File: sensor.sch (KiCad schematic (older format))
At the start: 82 parts, among them CON1 Micro USB, CON2 PROG, CON3 Jack-DC, Q1 BSS214N, Q2 BSS214N, Q3 BSS214N, Q4 BSS214N, Q5 BSS214N, Q6 BSS214N, SW1 RESET, SW2 CFG, U1 LM7805, U2 TLV1117LV33DCY, U3 ESP-12F, U4 HTU21D, U5 PMS7003

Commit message: Schematic finishing and cleanup.
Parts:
- added CON5: Conn_01x08, Connectors_Molex:Molex_PicoBlade_53048-0810_08x1.25mm_Angled, symbol Conn_01x08
- CON2: footprint Pin_Headers:Pin_Header_Angled_1x05_Pitch2.54mm -> Pin_Headers:Pin_Header_Straight_1x05_Pitch2.54mm
- CON3: footprint (none) -> Connectors:BARREL_JACK
- CON4: renamed from J?; footprint (none) -> Pin_Headers:Pin_Header_Straight_1x04_Pitch2.54mm
- SW1, SW2: footprint (none) -> Buttons_Switches_SMD:SW_SPST_EVQQ2
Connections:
- net +5V: now also CON5.1 (Pin_1)
- net GND: now also CON5.2 (Pin_2)
- net PMS_RXD: now also CON5.4 (Pin_4)
- net PMS_TXD: now also CON5.5 (Pin_5)
- net PMS_SET: now reaches R39.2, TP2.1, U5.10 (SET)
- net PMS_SET: now also CON5.3 (Pin_3)
- net PMS_RESET: now reaches R41.2, TP3.1, U5.5 (RESET)
- net PMS_RESET: now also CON5.6 (Pin_6)
- no-connect marks 9 -> 11
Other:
- note added: "Alternative connector for \nHTU21D module, can be used\nif assembling board by hand."
- note added: "Buttons"
- note added: "Connector for alternative\nPMS5003 sensor. Molex\n1.25mm PicoBlade\n530480810 or 530470810"
- note added: "HTU21D, HDC1080, Si7020 can be used.\nAccording to datasheet , central pad \nshould be left floating.\nCurrent consumption negligible."
- note added: "Humidity and temperature sensor"
- note added: "LEDs"
- note added: "Max 20mA per single LED @ minimum LED forward voltage and supply 5V+5%.\nMax. total current 200mA for one color, 600mA for all total on, but software\nlimited to 200mA max."
- note added: "Optional power supply input"
- note added: "Particulate matter sensor"
- note added: "Power supply"
- note added: "Programming connector"
- note added: "WiFi/processing module"
- note removed: "Alternative connector"
- note removed: "Humidity and temperature sensor.\nHTU21D, HDC1080, Si7020 can be used.\nAccording to datasheet , central pad \nshould be left floating.\nCurrent consumption negligible."
- note removed: "Max 20mA per single LED @ minimum LED forward voltage and supply 5V+5%.\nMax. total current 200mA for one color, 600mA for all total on."
- moved on the sheet: C1, C2, C3, C4, C5, C6, C7, C8, C9, CON1, CON2, CON3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

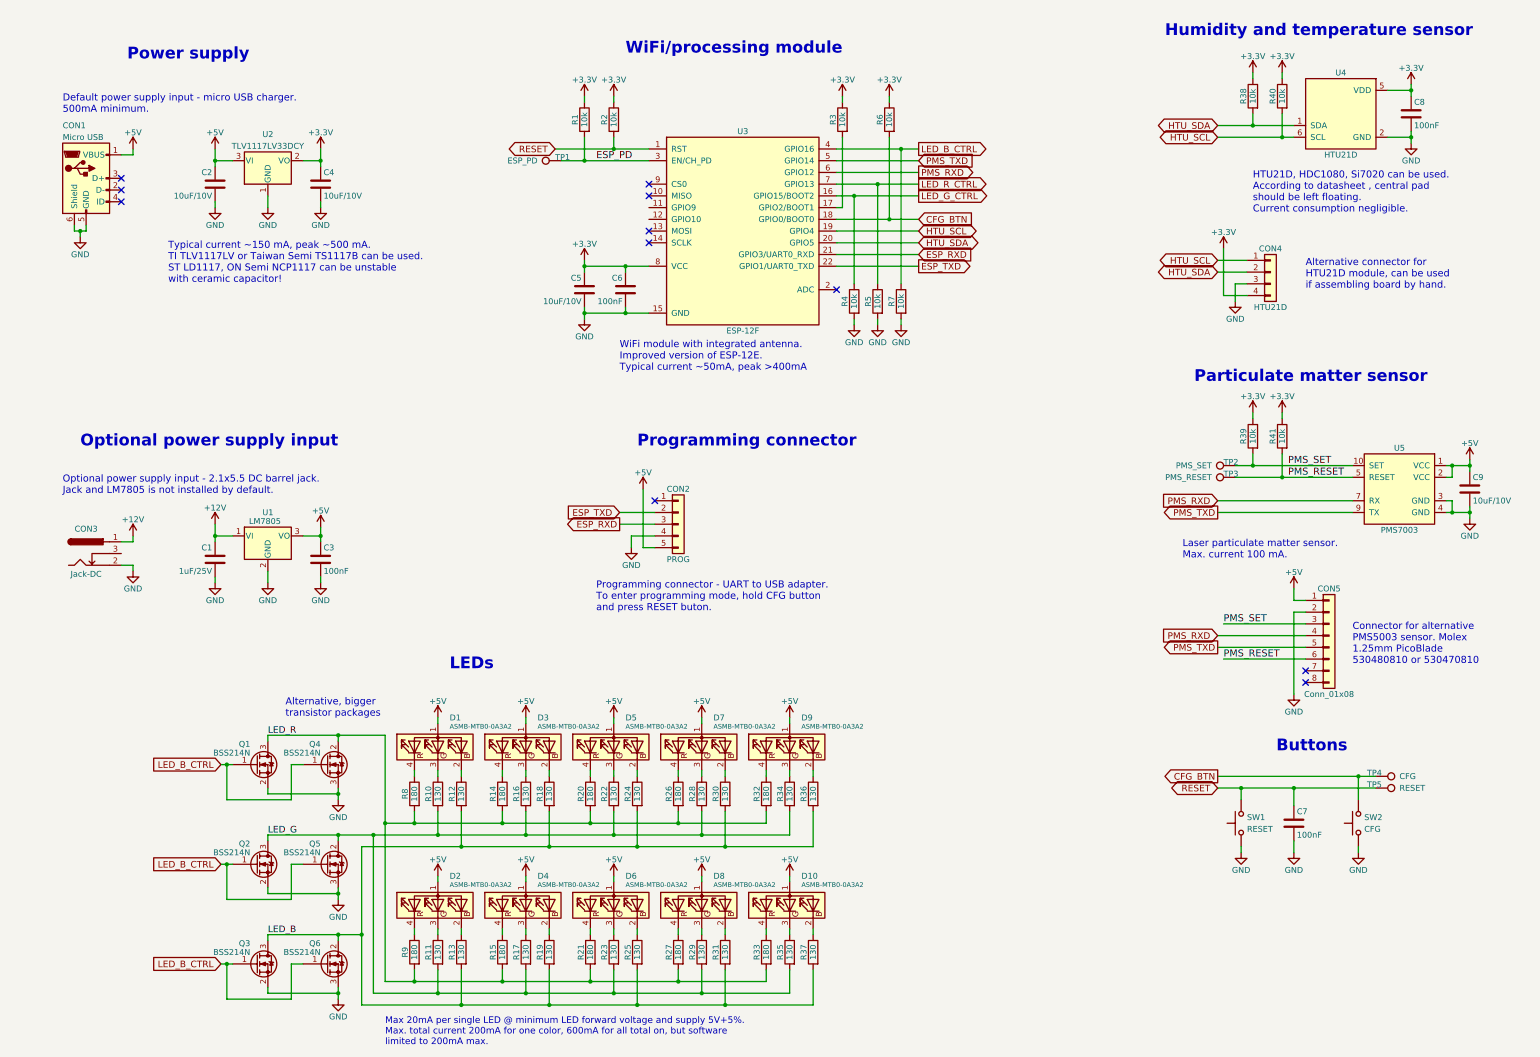
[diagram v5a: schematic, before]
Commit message: Fix ERC errors, add more testpoints.
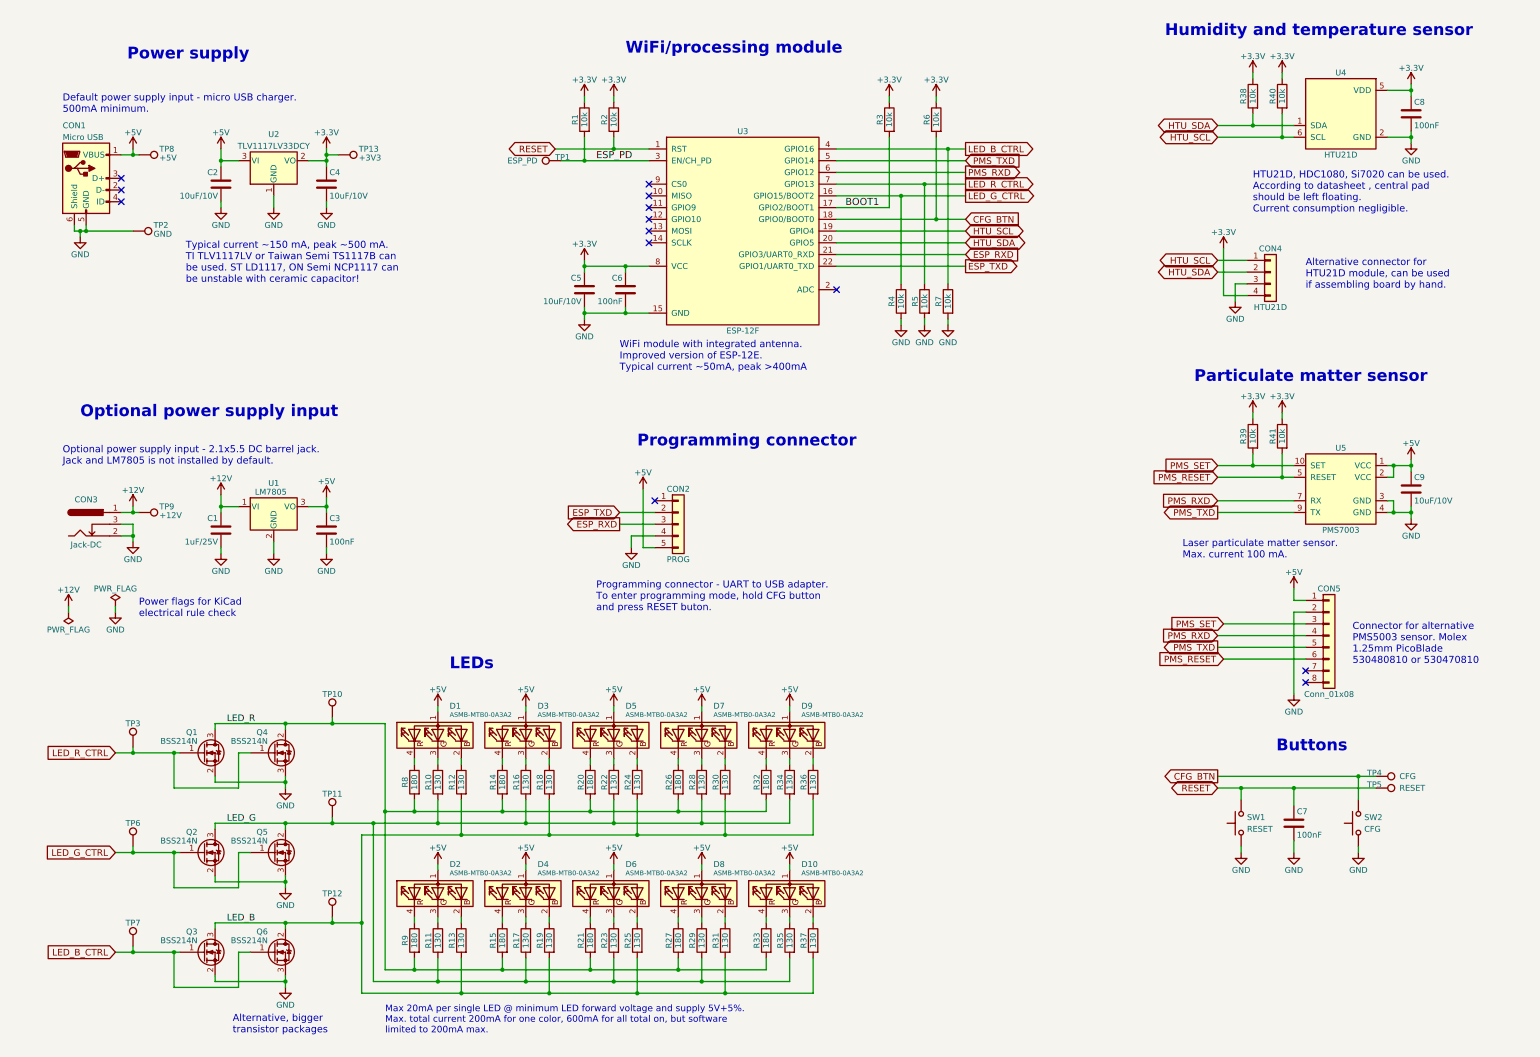
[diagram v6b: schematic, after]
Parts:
- added TP10, TP11, TP12, TP6, TP7: -, Wire_Pads:SolderWirePad_single_0-8mmDrill, symbol TEST_1P
- added TP13: +3V3, Wire_Pads:SolderWirePad_single_0-8mmDrill, symbol TEST_1P
- added TP8: +5V, Wire_Pads:SolderWirePad_single_0-8mmDrill, symbol TEST_1P
- added TP9: +12V, Wire_Pads:SolderWirePad_single_0-8mmDrill, symbol TEST_1P
- TP2: value PMS_SET -> GND
- TP3: value PMS_RESET -> -
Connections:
- net +12V: now also TP9.1
- net +3V3: now also TP13.1
- net +5V: now also TP8.1
- net GND: now also CON3.3, TP2.1
- net LED_B: now also TP12.1
- net LED_B_CTRL: now also TP7.1; no longer Q1.1 (G), Q2.1 (G), Q4.1 (G), Q5.1 (G)
- net LED_G: now also TP11.1
- net LED_G_CTRL: now also Q2.1 (G), Q5.1 (G), TP6.1
- net LED_R: now also TP10.1
- net LED_R_CTRL: now also Q1.1 (G), Q4.1 (G), TP3.1
- net PMS_RESET: no longer TP3.1
- net PMS_SET: no longer TP2.1
- net BOOT1: now reaches R3.2, U3.17 (GPIO2/BOOT1)
- no-connect marks 11 -> 13
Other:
- note added: "Power flags for KiCad\nelectrical rule check"
- note added: "Typical current ~~150 mA, peak ~~500 mA.\nTI TLV1117LV or Taiwan Semi TS1117B can \nbe used. ST LD1117, ON Semi NCP1117 can \nbe unstable with ceramic capacitor!"
- note removed: "Typical current ~~150 mA, peak ~~500 mA.\nTI TLV1117LV or Taiwan Semi TS1117B can be used.\nST LD1117, ON Semi NCP1117 can be unstable \nwith ceramic capacitor!"
- moved on the sheet: C1, C2, C3, C4, C9, CON3, D1, D10, D2, D3, D4, D5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

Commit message: Initial draft PCB placement
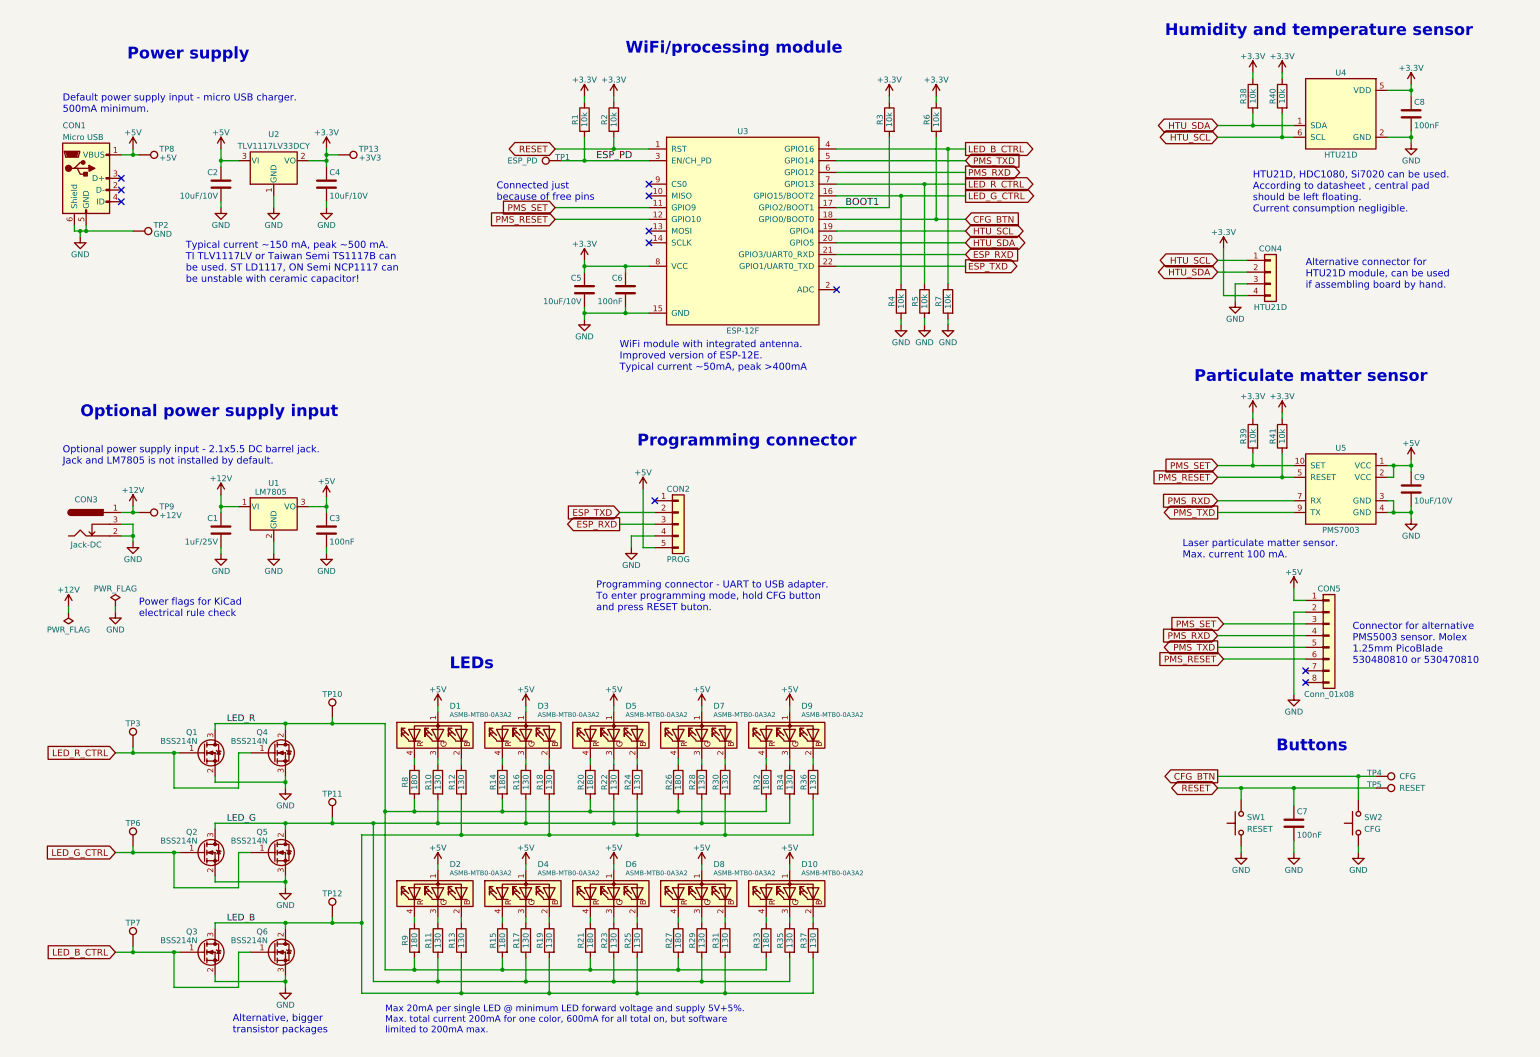
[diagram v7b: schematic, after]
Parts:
- U3: footprint RF_Modules:ESP-12E -> less-smog:ESP-12F
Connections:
- net PMS_RESET: now also U3.12 (GPIO10)
- net PMS_SET: now also U3.11 (GPIO9)
- no-connect marks 13 -> 11
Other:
- note added: "Connected just \nbecause of free pins"

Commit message: Change some footprint pads to bigger ones.
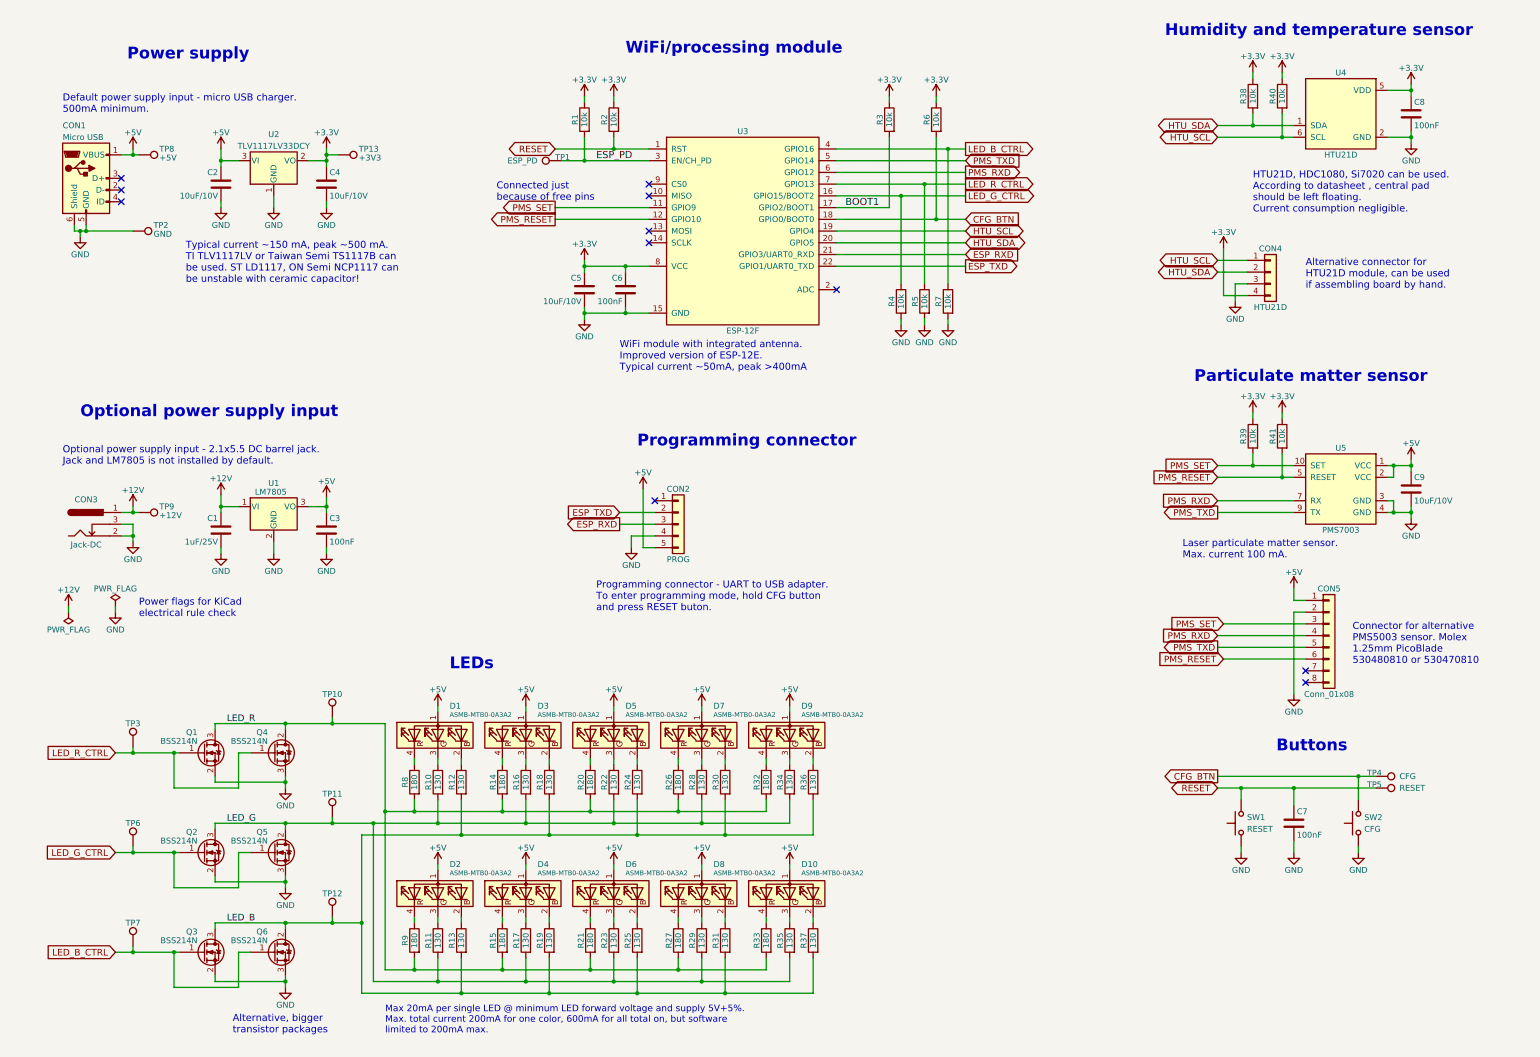
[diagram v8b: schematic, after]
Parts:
- C1, C2, C3, C4, C5, C6, C7, C8, C9: footprint Capacitors_SMD:C_0805 -> less-smog:C_0805
- CON5: footprint Connectors_Molex:Molex_PicoBlade_53048-0810_08x1.25mm_Angled -> less-smog:Molex_PicoBlade_53048-0810
- Q1, Q2, Q3: footprint TO_SOT_Packages_SMD:SOT-23 -> less-smog:SOT-23
- R1, R10, R11, R12, R13, R14, R15, R16, R17, R18, R19, R2, R20, R21, R22, R23, R24, R25, R26, R27, R28, R29, R3, R30, R31, R32, R33, R34, R35, R36, R37, R38, R39, R4, R40, R41, R5, R6, R7, R8, R9: footprint Resistors_SMD:R_1206 -> less-smog:R_1206
- SW1, SW2: footprint Buttons_Switches_SMD:SW_SPST_EVQQ2 -> less-smog:MicroswitchSmd-4.3_N
